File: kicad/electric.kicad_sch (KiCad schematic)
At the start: 1 part

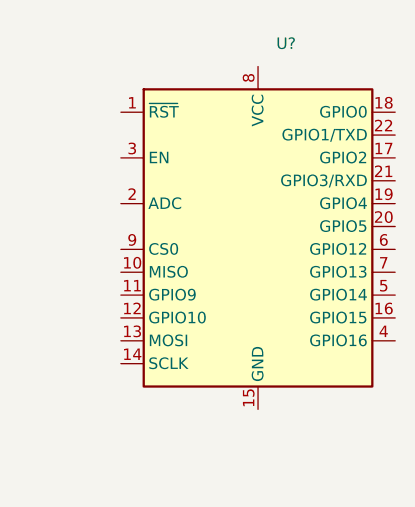
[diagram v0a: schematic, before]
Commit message: feat(kicad): added external esp8266 schema lib
Signed-off-by: Mario-F <github@fritschen.net>
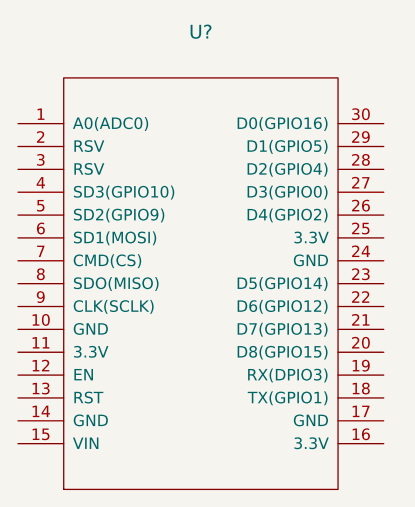
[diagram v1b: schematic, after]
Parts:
- removed U?: (no value), symbol RF_Module:ESP-12E
- added U?: (no value), symbol ESP8266:NodeMCU1.0(ESP-12E)
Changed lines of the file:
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@@
 (kicad_sch (version 20211123) (generator eeschema)
   (paper "A4")
-  (symbol (lib_id "RF_Module:ESP-12E") (at 147.32 91.44 0) (unit 1)
+  (symbol (lib_id "ESP8266:NodeMCU1.0(ESP-12E)") (at 140.97 95.25 0) (unit 1)
     (in_bom yes) (on_board yes) (fields_autoplaced)
-    (property "Reference" "U?" (id 0) (at 149.3394 68.58 0)
-      (effects (font (size 1.27 1.27)) (justify left))
+    (property "Reference" "U?" (id 0) (at 140.97 67.31 0)
+      (effects (font (size 1.524 1.524)))
     )
-    (property "Value" "" (id 1) (at 149.3394 71.12 0)
-      (effects (font (size 1.27 1.27)) (justify left))
+    (property "Value" "" (id 1) (at 140.97 71.12 0)
+      (effects (font (size 1.524 1.524)))
     )
-    (property "Footprint" "" (id 2) (at 147.32 91.44 0)
-      (effects (font (size 1.27 1.27)) hide)
+    (property "Footprint" "" (id 2) (at 125.73 116.84 0)
+      (effects (font (size 1.524 1.524)))
     )
-    (property "Datasheet" "http://wiki.ai-thinker.com/_media/esp8266/esp8266_series_modules_user_manual_v1.1.pdf" (id 3) (at 138.43 88.9 0)
-      (effects (font (size 1.27 1.27)) hide)
+    (property "Datasheet" "" (id 3) (at 125.73 116.84 0)
+      (effects (font (size 1.524 1.524)))
     )
     (pin "1")
@@
     (pin "21")
     (pin "22")
+    (pin "23")
+    (pin "24")
+    (pin "25")
+    (pin "26")
+    (pin "27")
+    (pin "28")
+    (pin "29")
     (pin "3")
+    (pin "30")
     (pin "4")
     (pin "5")
@@
   )
   (symbol_instances
-    (path "/1b1d0345-1365-4862-a6df-51ce483281a8"
-      (reference "U?") (unit 1) (value "ESP-12E") (footprint "RF_Module:ESP-12E")
+    (path "/4244f2cf-53fb-48c6-88ac-de581a83aeb5"
+      (reference "U?") (unit 1) (value "NodeMCU1.0(ESP-12E)") (footprint "")
     )
   )

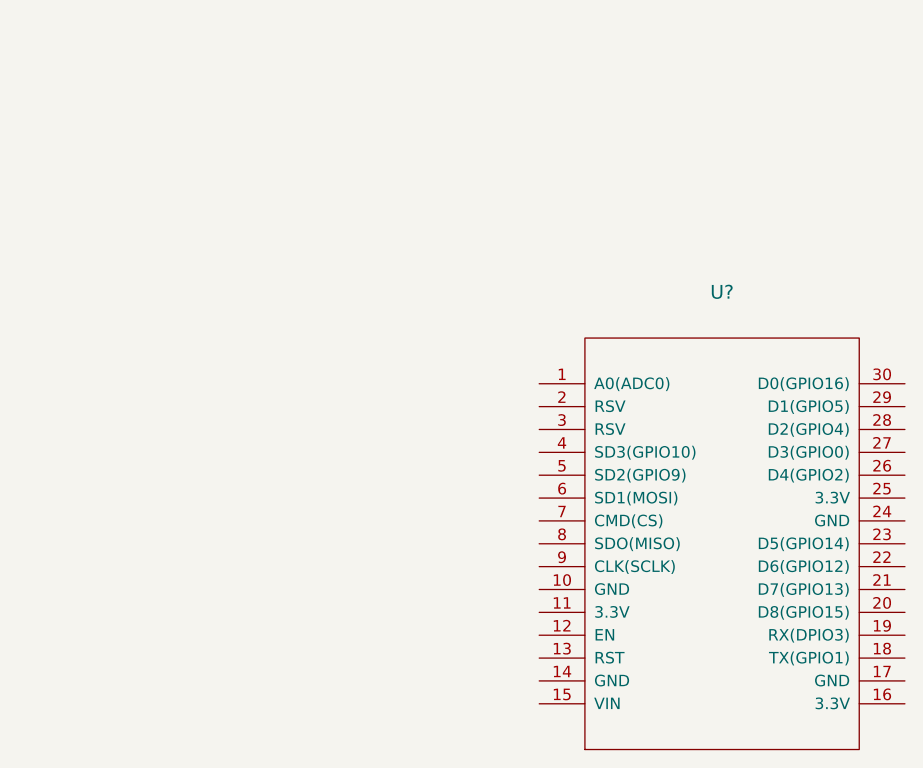
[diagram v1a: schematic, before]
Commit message: feat(kicad): added power supply
Signed-off-by: Mario-F <github@fritschen.net>
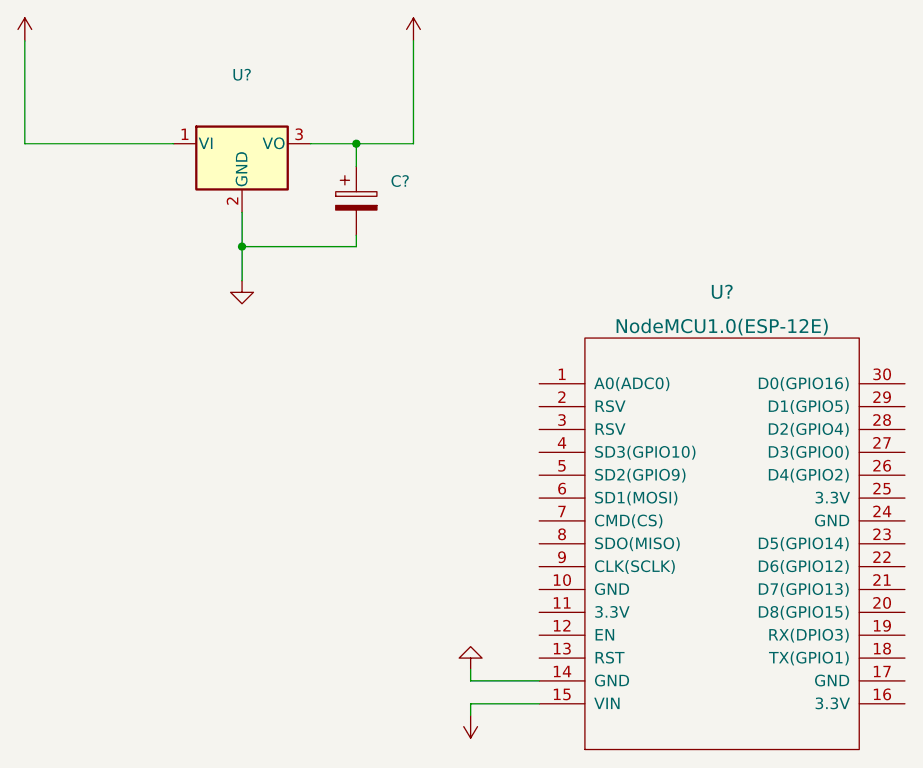
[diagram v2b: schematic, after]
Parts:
- added C?: (no value), symbol Device:C_Polarized
- added U?: (no value), symbol Regulator_Linear:LM7805_TO220
- U?: value (none) -> NodeMCU1.0(ESP-12E)
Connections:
- net GND: now reaches U?.14 (GND)
- net GND: now also C?.2, U?.2 (GND)
- net +5V: now reaches U?.15 (VIN)
- net +5V: now also C?.1, U?.3 (VO)
- new net +12V: U?.1 (VI)
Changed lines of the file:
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@@
 (kicad_sch (version 20211123) (generator eeschema)
   (paper "A4")
+  (junction (at 87.63 62.23) (diameter 0) (color 0 0 0 0)
+  )
+  (junction (at 100.33 50.8) (diameter 0) (color 0 0 0 0)
+  )
+  (wire (pts (xy 100.33 60.96) (xy 100.33 62.23))
+    (stroke (width 0) (type default) (color 0 0 0 0))
+  )
+  (wire (pts (xy 113.03 109.22) (xy 113.03 110.49))
+    (stroke (width 0) (type default) (color 0 0 0 0))
+  )
+  (wire (pts (xy 113.03 114.3) (xy 113.03 113.03))
+    (stroke (width 0) (type default) (color 0 0 0 0))
+  )
+  (wire (pts (xy 106.68 50.8) (xy 106.68 39.37))
+    (stroke (width 0) (type default) (color 0 0 0 0))
+  )
+  (wire (pts (xy 87.63 62.23) (xy 87.63 66.04))
+    (stroke (width 0) (type default) (color 0 0 0 0))
+  )
+  (wire (pts (xy 113.03 110.49) (xy 120.65 110.49))
+    (stroke (width 0) (type default) (color 0 0 0 0))
+  )
+  (wire (pts (xy 87.63 62.23) (xy 100.33 62.23))
+    (stroke (width 0) (type default) (color 0 0 0 0))
+  )
+  (wire (pts (xy 87.63 58.42) (xy 87.63 62.23))
+    (stroke (width 0) (type default) (color 0 0 0 0))
+  )
+  (wire (pts (xy 95.25 50.8) (xy 100.33 50.8))
+    (stroke (width 0) (type default) (color 0 0 0 0))
+  )
+  (wire (pts (xy 63.5 39.37) (xy 63.5 50.8))
+    (stroke (width 0) (type default) (color 0 0 0 0))
+  )
+  (wire (pts (xy 100.33 50.8) (xy 100.33 53.34))
+    (stroke (width 0) (type default) (color 0 0 0 0))
+  )
+  (wire (pts (xy 113.03 113.03) (xy 120.65 113.03))
+    (stroke (width 0) (type default) (color 0 0 0 0))
+  )
+  (wire (pts (xy 100.33 50.8) (xy 106.68 50.8))
+    (stroke (width 0) (type default) (color 0 0 0 0))
+  )
+  (wire (pts (xy 63.5 50.8) (xy 80.01 50.8))
+    (stroke (width 0) (type default) (color 0 0 0 0))
+  )
+  (symbol (lib_id "power:+5V") (at 113.03 114.3 180) (unit 1)
+    (in_bom yes) (on_board yes) (fields_autoplaced)
+    (property "Reference" "#PWR?" (id 0) (at 113.03 110.49 0)
+      (effects (font (size 1.27 1.27)) hide)
+    )
+    (property "Value" "" (id 1) (at 113.03 119.38 0))
+    (property "Footprint" "" (id 2) (at 113.03 114.3 0)
+      (effects (font (size 1.27 1.27)) hide)
+    )
+    (property "Datasheet" "" (id 3) (at 113.03 114.3 0)
+      (effects (font (size 1.27 1.27)) hide)
+    )
+    (pin "1")
+  )
   (symbol (lib_id "ESP8266:NodeMCU1.0(ESP-12E)") (at 140.97 95.25 0) (unit 1)
     (in_bom yes) (on_board yes) (fields_autoplaced)
@@
       (effects (font (size 1.524 1.524)))
     )
-    (property "Value" "" (id 1) (at 140.97 71.12 0)
+    (property "Value" "NodeMCU1.0(ESP-12E)" (id 1) (at 140.97 71.12 0)
       (effects (font (size 1.524 1.524)))
     )
@@
     (pin "9")
   )
+  (symbol (lib_id "power:+5V") (at 106.68 39.37 0) (unit 1)
+    (in_bom yes) (on_board yes) (fields_autoplaced)
+    (property "Reference" "#PWR?" (id 0) (at 106.68 43.18 0)
+      (effects (font (size 1.27 1.27)) hide)
+    )
+    (property "Value" "" (id 1) (at 106.68 34.29 0))
+    (property "Footprint" "" (id 2) (at 106.68 39.37 0)
+      (effects (font (size 1.27 1.27)) hide)
+    )
+    (property "Datasheet" "" (id 3) (at 106.68 39.37 0)
+      (effects (font (size 1.27 1.27)) hide)
+    )
+    (pin "1")
+  )
+  (symbol (lib_id "Device:C_Polarized") (at 100.33 57.15 0) (unit 1)
+    (in_bom yes) (on_board yes) (fields_autoplaced)
+    (property "Reference" "C?" (id 0) (at 104.14 54.9909 0)
+      (effects (font (size 1.27 1.27)) (justify left))
+    )
+    (property "Value" "" (id 1) (at 104.14 57.5309 0)
+      (effects (font (size 1.27 1.27)) (justify left))
+    )
+    (property "Footprint" "" (id 2) (at 101.2952 60.96 0)
+      (effects (font (size 1.27 1.27)) hide)
+    )
+    (property "Datasheet" "~" (id 3) (at 100.33 57.15 0)
+      (effects (font (size 1.27 1.27)) hide)
+    )
+    (pin "1")
+    (pin "2")
+  )
+  (symbol (lib_id "power:GND") (at 87.63 66.04 0) (unit 1)
+    (in_bom yes) (on_board yes) (fields_autoplaced)
+    (property "Reference" "#PWR?" (id 0) (at 87.63 72.39 0)
+      (effects (font (size 1.27 1.27)) hide)
+    )
+    (property "Value" "" (id 1) (at 87.63 71.12 0))
+    (property "Footprint" "" (id 2) (at 87.63 66.04 0)
+      (effects (font (size 1.27 1.27)) hide)
+    )
+    (property "Datasheet" "" (id 3) (at 87.63 66.04 0)
+      (effects (font (size 1.27 1.27)) hide)
+    )
+    (pin "1")
+  )
+  (symbol (lib_id "power:GND") (at 113.03 109.22 180) (unit 1)
+    (in_bom yes) (on_board yes) (fields_autoplaced)
+    (property "Reference" "#PWR?" (id 0) (at 113.03 102.87 0)
+      (effects (font (size 1.27 1.27)) hide)
+    )
+    (property "Value" "" (id 1) (at 113.03 104.14 0))
+    (property "Footprint" "" (id 2) (at 113.03 109.22 0)
+      (effects (font (size 1.27 1.27)) hide)
+    )
+    (property "Datasheet" "" (id 3) (at 113.03 109.22 0)
+      (effects (font (size 1.27 1.27)) hide)
+    )
+    (pin "1")
+  )
+  (symbol (lib_id "power:+12V") (at 63.5 39.37 0) (unit 1)
+    (in_bom yes) (on_board yes) (fields_autoplaced)
+    (property "Reference" "#PWR?" (id 0) (at 63.5 43.18 0)
+      (effects (font (size 1.27 1.27)) hide)
+    )
+    (property "Value" "" (id 1) (at 63.5 34.29 0))
+    (property "Footprint" "" (id 2) (at 63.5 39.37 0)
+      (effects (font (size 1.27 1.27)) hide)
+    )
+    (property "Datasheet" "" (id 3) (at 63.5 39.37 0)
+      (effects (font (size 1.27 1.27)) hide)
+    )
+    (pin "1")
+  )
+  (symbol (lib_id "Regulator_Linear:LM7805_TO220") (at 87.63 50.8 0) (unit 1)
+    (in_bom yes) (on_board yes) (fields_autoplaced)
+    (property "Reference" "U?" (id 0) (at 87.63 43.18 0))
+    (property "Value" "" (id 1) (at 87.63 45.72 0))
+    (property "Footprint" "" (id 2) (at 87.63 45.085 0)
+      (effects (font (size 1.27 1.27) italic) hide)
+    )
+    (property "Datasheet" "https://www.onsemi.cn/PowerSolutions/document/MC7800-D.PDF" (id 3) (at 87.63 52.07 0)
+      (effects (font (size 1.27 1.27)) hide)
+    )
+    (pin "1")
+    (pin "2")
+    (pin "3")
+  )
   (sheet_instances
     (path "/" (page "1"))
   )
   (symbol_instances
+    (path "/3f5b974d-3ce2-419c-90a4-87dd9099b68f"
+      (reference "#PWR?") (unit 1) (value "+5V") (footprint "")
+    )
+    (path "/4efa236a-0cac-4446-9fe1-6087fcb3e483"
+      (reference "#PWR?") (unit 1) (value "+5V") (footprint "")
+    )
+    (path "/9ec3048f-a2b1-4a62-93ca-107041eae2bc"
+      (reference "#PWR?") (unit 1) (value "GND") (footprint "")
+    )
+    (path "/c6f95339-135c-4964-80f4-20dc2c5ebd9f"
+      (reference "#PWR?") (unit 1) (value "GND") (footprint "")
+    )
+    (path "/e50581fd-8281-401f-a1ac-ca31ebad78d8"
+      (reference "#PWR?") (unit 1) (value "+12V") (footprint "")
+    )
+    (path "/9c3fc60c-3c32-41f8-9eaa-cf0d9df0f7a0"
+      (reference "C?") (unit 1) (value "C_Polarized") (footprint "")
+    )
     (path "/4244f2cf-53fb-48c6-88ac-de581a83aeb5"
       (reference "U?") (unit 1) (value "NodeMCU1.0(ESP-12E)") (footprint "")
     )
-  )
+    (path "/e997c615-0a9d-46fc-872f-6b2d14f01b36"
+      (reference "U?") (unit 1) (value "LM7805_TO220") (footprint "Package_TO_SOT_THT:TO-220-3_Vertical")
+    )
+  )

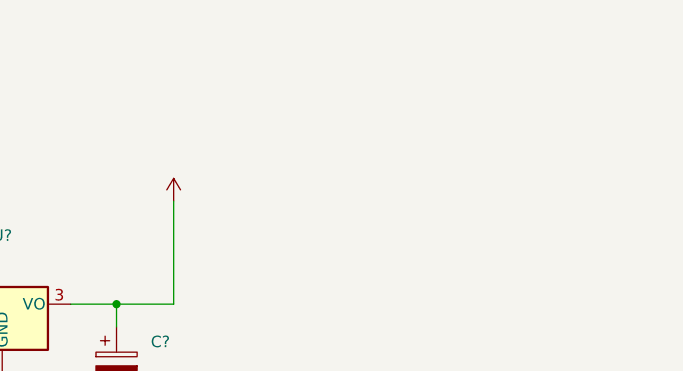
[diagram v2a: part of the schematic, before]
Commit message: feat(kicad): added main power connector
Signed-off-by: Mario-F <github@fritschen.net>
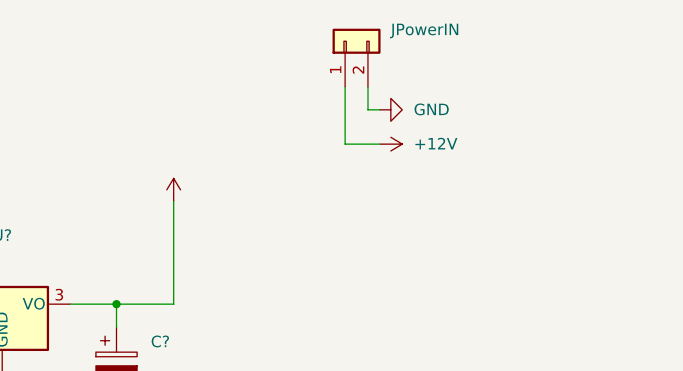
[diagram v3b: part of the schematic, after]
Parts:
- added JPowerIN: (no value), symbol Connector_Generic:Conn_01x02
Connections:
- net +12V: now also JPowerIN.1 (Pin_1)
- net GND: now also JPowerIN.2 (Pin_2)
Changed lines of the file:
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@@
+    (stroke (width 0) (type default) (color 0 0 0 0))
+  )
+  (wire (pts (xy 128.27 26.67) (xy 128.27 29.21))
     (stroke (width 0) (type default) (color 0 0 0 0))
   )
@@
     (stroke (width 0) (type default) (color 0 0 0 0))
   )
+  (wire (pts (xy 125.73 33.02) (xy 129.54 33.02))
+    (stroke (width 0) (type default) (color 0 0 0 0))
+  )
   (wire (pts (xy 63.5 39.37) (xy 63.5 50.8))
     (stroke (width 0) (type default) (color 0 0 0 0))
   )
+  (wire (pts (xy 125.73 26.67) (xy 125.73 33.02))
+    (stroke (width 0) (type default) (color 0 0 0 0))
+  )
   (wire (pts (xy 100.33 50.8) (xy 100.33 53.34))
     (stroke (width 0) (type default) (color 0 0 0 0))
   )
+  (wire (pts (xy 128.27 29.21) (xy 129.54 29.21))
+    (stroke (width 0) (type default) (color 0 0 0 0))
+  )
   (wire (pts (xy 113.03 113.03) (xy 120.65 113.03))
     (stroke (width 0) (type default) (color 0 0 0 0))
@@
   (wire (pts (xy 63.5 50.8) (xy 80.01 50.8))
     (stroke (width 0) (type default) (color 0 0 0 0))
+  )
+  (symbol (lib_id "power:GND") (at 129.54 29.21 90) (unit 1)
+    (in_bom yes) (on_board yes) (fields_autoplaced)
+    (property "Reference" "#PWR?" (id 0) (at 135.89 29.21 0)
+      (effects (font (size 1.27 1.27)) hide)
+    )
+    (property "Value" "GND" (id 1) (at 133.35 29.2099 90)
+      (effects (font (size 1.27 1.27)) (justify right))
+    )
+    (property "Footprint" "" (id 2) (at 129.54 29.21 0)
+      (effects (font (size 1.27 1.27)) hide)
+    )
+    (property "Datasheet" "" (id 3) (at 129.54 29.21 0)
+      (effects (font (size 1.27 1.27)) hide)
+    )
+    (pin "1")
   )
   (symbol (lib_id "power:+5V") (at 113.03 114.3 180) (unit 1)
@@
     (pin "9")
   )
+  (symbol (lib_id "Connector_Generic:Conn_01x02") (at 125.73 21.59 90) (unit 1)
+    (in_bom yes) (on_board yes) (fields_autoplaced)
+    (property "Reference" "JPowerIN" (id 0) (at 130.81 20.3199 90)
+      (effects (font (size 1.27 1.27)) (justify right))
+    )
+    (property "Value" "" (id 1) (at 130.81 22.8599 90)
+      (effects (font (size 1.27 1.27)) (justify right))
+    )
+    (property "Footprint" "" (id 2) (at 125.73 21.59 0)
+      (effects (font (size 1.27 1.27)) hide)
+    )
+    (property "Datasheet" "~" (id 3) (at 125.73 21.59 0)
+      (effects (font (size 1.27 1.27)) hide)
+    )
+    (pin "1")
+    (pin "2")
+  )
   (symbol (lib_id "power:+5V") (at 106.68 39.37 0) (unit 1)
     (in_bom yes) (on_board yes) (fields_autoplaced)
@@
     )
     (property "Datasheet" "" (id 3) (at 87.63 66.04 0)
+      (effects (font (size 1.27 1.27)) hide)
+    )
+    (pin "1")
+  )
+  (symbol (lib_id "power:+12V") (at 129.54 33.02 270) (unit 1)
+    (in_bom yes) (on_board yes) (fields_autoplaced)
+    (property "Reference" "#PWR?" (id 0) (at 125.73 33.02 0)
+      (effects (font (size 1.27 1.27)) hide)
+    )
+    (property "Value" "+12V" (id 1) (at 133.35 33.0199 90)
+      (effects (font (size 1.27 1.27)) (justify left))
+    )
+    (property "Footprint" "" (id 2) (at 129.54 33.02 0)
+      (effects (font (size 1.27 1.27)) hide)
+    )
+    (property "Datasheet" "" (id 3) (at 129.54 33.02 0)
       (effects (font (size 1.27 1.27)) hide)
     )
@@
   )
   (symbol_instances
+    (path "/278c8023-393b-4d07-b78b-27523f3cebe8"
+      (reference "#PWR?") (unit 1) (value "GND") (footprint "")
+    )
     (path "/3f5b974d-3ce2-419c-90a4-87dd9099b68f"
       (reference "#PWR?") (unit 1) (value "+5V") (footprint "")
@@
       (reference "#PWR?") (unit 1) (value "GND") (footprint "")
     )
+    (path "/bca2a5a0-a558-414e-85ec-0cc8a111f6b7"
+      (reference "#PWR?") (unit 1) (value "+12V") (footprint "")
+    )
     (path "/c6f95339-135c-4964-80f4-20dc2c5ebd9f"
       (reference "#PWR?") (unit 1) (value "GND") (footprint "")
@@
       (reference "C?") (unit 1) (value "C_Polarized") (footprint "")
     )
+    (path "/446a4d7a-e7f1-4200-bae1-5b36895d93d9"
+      (reference "JPowerIN") (unit 1) (value "Conn_01x02") (footprint "")
+    )
     (path "/4244f2cf-53fb-48c6-88ac-de581a83aeb5"
